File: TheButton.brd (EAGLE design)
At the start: 38.7 x 42.9 mm, 24 parts, among them IC1 74HC595N, IC2 REG1117

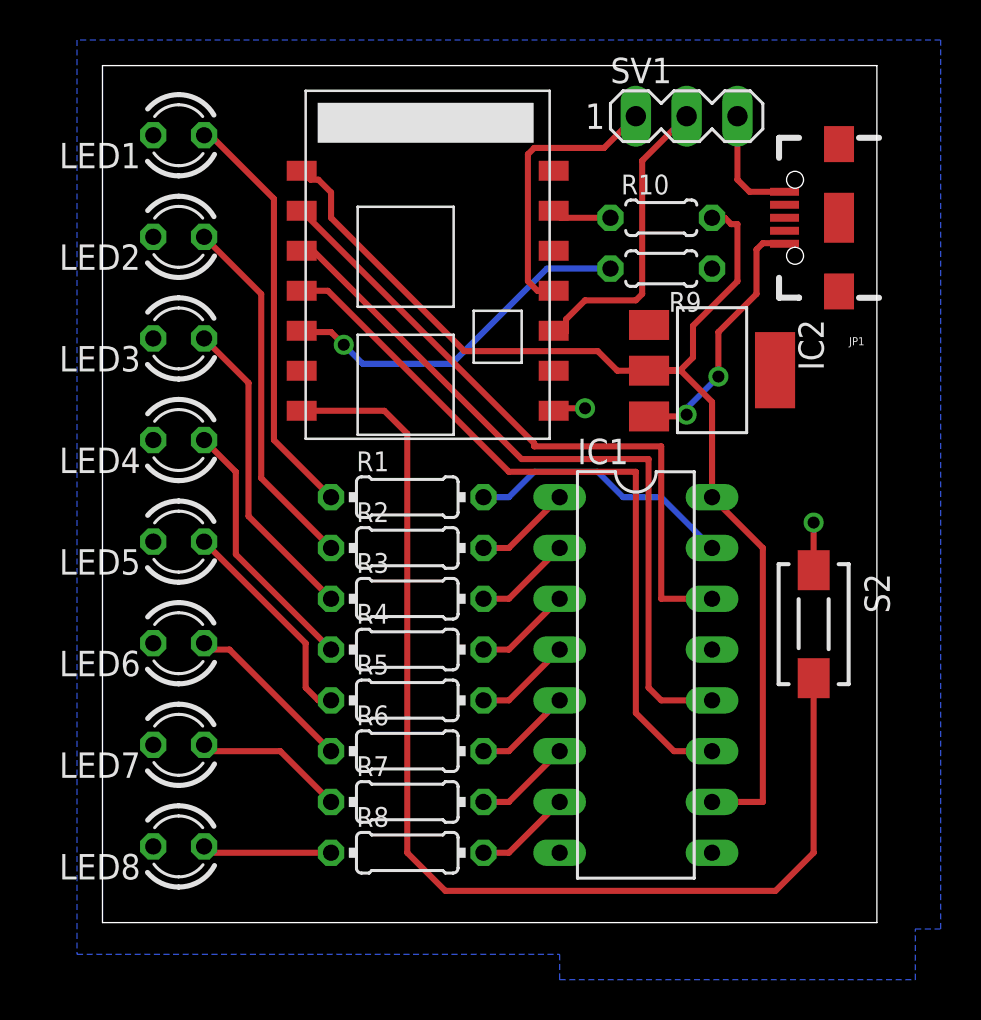
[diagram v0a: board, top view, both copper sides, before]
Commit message: Added png Changed USB-contat to SMD only version
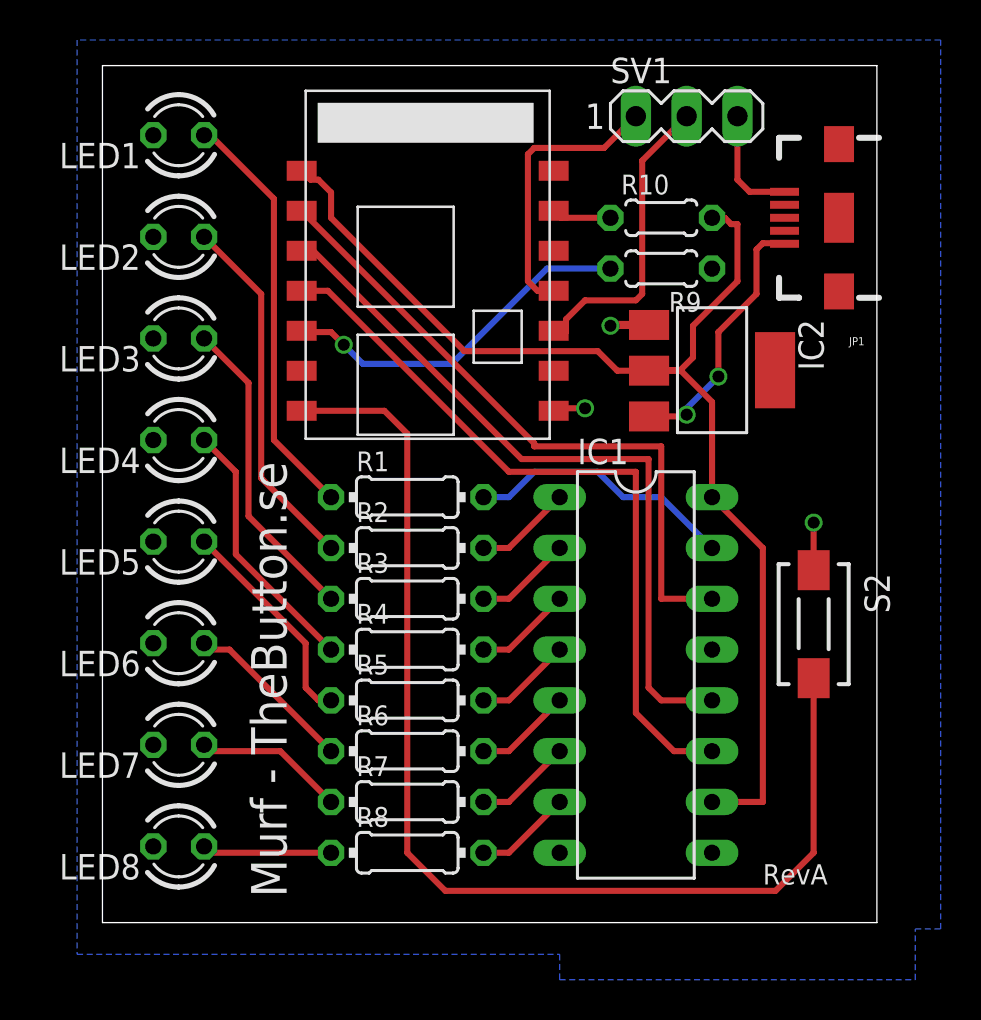
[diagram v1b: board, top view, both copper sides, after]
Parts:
- JP1: device SparkFun-Connectors:USB-B-MICRO-SMD_V03 -> Murf:USB-B-MICRO-SMD_V03
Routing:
- net GND: track 9.78 -> 11.8 mm, vias 2 -> 3
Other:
- board text added: "Murf - TheButton.se"
- board text added: "RevA"
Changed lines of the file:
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@@
 <wire x1="38.7225" y1="42.8525" x2="0" y2="42.8525" width="0" layer="20"/>
 <wire x1="0" y1="42.8525" x2="0" y2="0" width="0" layer="20"/>
+<text x="9.2075" y="1.27" size="1.778" layer="21" rot="R90">Murf - TheButton.se</text>
+<text x="33.02" y="1.905" size="1.016" layer="21">RevA</text>
 </plain>
 <attributes>
@@
 </class>
 </classes>
-<designrules name="default">
+<designrules name="smart-prototyping.com.EagleRules">
 <description language="de">&lt;b&gt;EAGLE Design Rules&lt;/b&gt;
 &lt;p&gt;
@@
 necessary adjustments and save your customized
 design rules under a new name.</description>
+<description language="zh">&lt;b&gt;NOA-Labs EAGLE Design Rules&lt;/b&gt;
+</description>
 <param name="layerSetup" value="(1*16)"/>
 <param name="mtCopper" value="0.035mm 0.035mm 0.035mm 0.035mm 0.035mm 0.035mm 0.035mm 0.035mm 0.035mm 0.035mm 0.035mm 0.035mm 0.035mm 0.035mm 0.035mm 0.035mm"/>
 <param name="mtIsolate" value="1.5mm 0.15mm 0.2mm 0.15mm 0.2mm 0.15mm 0.2mm 0.15mm 0.2mm 0.15mm 0.2mm 0.15mm 0.2mm 0.15mm 0.2mm"/>
-<param name="mdWireWire" value="8mil"/>
-<param name="mdWirePad" value="8mil"/>
-<param name="mdWireVia" value="8mil"/>
-<param name="mdPadPad" value="8mil"/>
-<param name="mdPadVia" value="8mil"/>
-<param name="mdViaVia" value="8mil"/>
-<param name="mdSmdPad" value="8mil"/>
-<param name="mdSmdVia" value="8mil"/>
-<param name="mdSmdSmd" value="8mil"/>
+<param name="mdWireWire" value="7mil"/>
+<param name="mdWirePad" value="7mil"/>
+<param name="mdWireVia" value="7mil"/>
+<param name="mdPadPad" value="7mil"/>
+<param name="mdPadVia" value="7mil"/>
+<param name="mdViaVia" value="7mil"/>
+<param name="mdSmdPad" value="0mil"/>
+<param name="mdSmdVia" value="0mil"/>
+<param name="mdSmdSmd" value="0mil"/>
 <param name="mdViaViaSameLayer" value="8mil"/>
 <param name="mnLayersViaInSmd" value="2"/>
-<param name="mdCopperDimension" value="40mil"/>
-<param name="mdDrill" value="8mil"/>
+<param name="mdCopperDimension" value="20mil"/>
+<param name="mdDrill" value="10mil"/>
 <param name="mdSmdStop" value="0mil"/>
-<param name="msWidth" value="10mil"/>
-<param name="msDrill" value="24mil"/>
-<param name="msMicroVia" value="9.99mm"/>
+<param name="msWidth" value="7mil"/>
+<param name="msDrill" value="12mil"/>
+<param name="msMicroVia" value="12mil"/>
 <param name="msBlindViaRatio" value="0.5"/>
 <param name="rvPadTop" value="0.25"/>
@@
 <param name="rlMinPadBottom" value="10mil"/>
 <param name="rlMaxPadBottom" value="20mil"/>
-<param name="rlMinViaOuter" value="8mil"/>
+<param name="rlMinViaOuter" value="6mil"/>
 <param name="rlMaxViaOuter" value="20mil"/>
-<param name="rlMinViaInner" value="8mil"/>
+<param name="rlMinViaInner" value="6mil"/>
 <param name="rlMaxViaInner" value="20mil"/>
 <param name="rlMinMicroViaOuter" value="4mil"/>
@@
 <param name="psTop" value="-1"/>
 <param name="psBottom" value="-1"/>
-<param name="psFirst" value="-1"/>
+<param name="psFirst" value="0"/>
 <param name="psElongationLong" value="100"/>
 <param name="psElongationOffset" value="100"/>
 <param name="mvStopFrame" value="1"/>
 <param name="mvCreamFrame" value="0"/>
-<param name="mlMinStopFrame" value="4mil"/>
-<param name="mlMaxStopFrame" value="4mil"/>
+<param name="mlMinStopFrame" value="2mil"/>
+<param name="mlMaxStopFrame" value="2mil"/>
 <param name="mlMinCreamFrame" value="0mil"/>
 <param name="mlMaxCreamFrame" value="0mil"/>
-<param name="mlViaStopLimit" value="0mil"/>
+<param name="mlViaStopLimit" value="25mil"/>
 <param name="srRoundness" value="0"/>
 <param name="srMinRoundness" value="0mil"/>
@@
 <param name="checkAngle" value="0"/>
 <param name="checkFont" value="1"/>
-<param name="checkRestrict" value="1"/>
+<param name="checkRestrict" value="0"/>
 <param name="useDiameter" value="13"/>
 <param name="maxErrors" value="50"/>
@@
 <attribute name="OC_FARNELL" value="1097566" x="30.48" y="27.6225" size="1.778" layer="27" rot="R270" display="off"/>
 </element>
-<element name="JP1" library="SparkFun-Connectors" package="USB-B-MICRO-SMD_V03" value="Power" x="36.83" y="35.2425" rot="R180">
+<element name="JP1" library="Murf" package="USB-B-MICRO-SMD_V03" value="Power" x="36.83" y="35.2425" rot="R180">
 <attribute name="PROD_ID" value="CONN-11752" x="36.83" y="35.2425" size="1.778" layer="27" rot="R180" display="off"/>
 </element>
@@
 <via x="35.56" y="20.0025" extent="1-16" drill="0.6" shape="octagon"/>
 <wire x1="35.56" y1="20.0025" x2="35.56" y2="17.6225" width="0.3048" layer="1"/>
-<wire x1="30.48" y1="32.7025" x2="27.3304" y2="29.8831" width="0" layer="19" extent="1-1"/>
+<wire x1="27.3304" y1="29.8831" x2="25.4" y2="29.8831" width="0.4064" layer="1"/>
+<wire x1="25.4" y1="29.8831" x2="25.4" y2="29.845" width="0.4064" layer="1"/>
+<via x="25.4" y="29.845" extent="1-16" drill="0.6" shape="square"/>
 </signal>
 <signal name="N$9">
